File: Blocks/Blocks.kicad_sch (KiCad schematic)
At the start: 0 parts

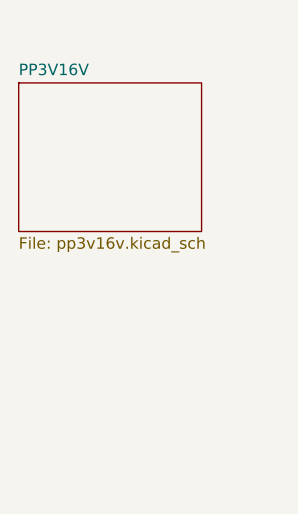
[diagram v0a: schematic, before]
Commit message: drop powermux
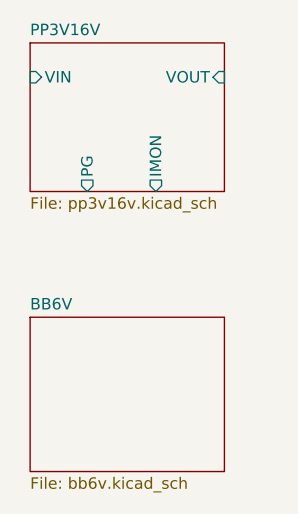
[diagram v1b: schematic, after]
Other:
- added sheet BB6V (bb6v.kicad_sch)
- sheet PP3V16V ports: added IMON, PG, VIN, VOUT; removed none
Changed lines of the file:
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@@
 	(paper "A4")
 	(sheet
-		(at 19.05 23.495)
-		(size 20.32 16.51)
+		(at 20.32 49.53)
+		(size 21.59 17.145)
+		(fields_autoplaced yes)
+		(stroke
+			(width 0.1524)
+			(type solid)
+		)
+		(fill
+			(color 0 0 0 0.0000)
+		)
+		(property "Sheetname" "BB6V"
+			(at 20.32 48.8184 0)
+			(effects
+				(font
+					(size 1.27 1.27)
+				)
+				(justify left bottom)
+			)
+		)
+		(property "Sheetfile" "bb6v.kicad_sch"
+			(at 20.32 67.2596 0)
+			(effects
+				(font
+					(size 1.27 1.27)
+				)
+				(justify left top)
+			)
+		)
+		(instances
+			(project "Blocks"
+				(path "/48ddfdd8-68fa-4e63-aa18-bc113cdf8cfa"
+					(page "3")
+				)
+			)
+		)
+	)
+	(sheet
+		(at 20.32 19.05)
+		(size 21.59 16.51)
 		(fields_autoplaced yes)
 		(stroke
@@
 		)
 		(property "Sheetname" "PP3V16V"
-			(at 19.05 22.7834 0)
+			(at 20.32 18.3384 0)
 			(effects
 				(font
@@
 		)
 		(property "Sheetfile" "pp3v16v.kicad_sch"
-			(at 19.05 40.5896 0)
+			(at 20.32 36.1446 0)
 			(effects
 				(font
@@
 			)
 		)
+		(pin "VIN" input
+			(at 20.32 22.86 180)
+			(effects
+				(font
+					(size 1.27 1.27)
+				)
+				(justify left)
+			)
+		)
+		(pin "PG" output
+			(at 26.67 35.56 270)
+			(effects
+				(font
+					(size 1.27 1.27)
+				)
+				(justify left)
+			)
+		)
+		(pin "VOUT" input
+			(at 41.91 22.86 0)
+			(effects
+				(font
+					(size 1.27 1.27)
+				)
+				(justify right)
+			)
+		)
+		(pin "IMON" output
+			(at 34.29 35.56 270)
+			(effects
+				(font
+					(size 1.27 1.27)
+				)
+				(justify left)
+			)
+		)

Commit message: BuckBoostTest v0.1
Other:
- sheet BB6V ports: added PG, VIN, VLogic, VOUT; removed none
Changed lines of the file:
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@@
+			)
+		)
+		(pin "VIN" input
+			(at 20.32 54.61 180)
+			(effects
+				(font
+					(size 1.27 1.27)
+				)
+				(justify left)
+			)
+		)
+		(pin "VOUT" input
+			(at 41.91 54.61 0)
+			(effects
+				(font
+					(size 1.27 1.27)
+				)
+				(justify right)
+			)
+		)
+		(pin "VLogic" input
+			(at 27.94 66.675 270)
+			(effects
+				(font
+					(size 1.27 1.27)
+				)
+				(justify left)
+			)
+		)
+		(pin "PG" output
+			(at 33.02 66.675 270)
+			(effects
+				(font
+					(size 1.27 1.27)
+				)
+				(justify left)
 			)
 		)

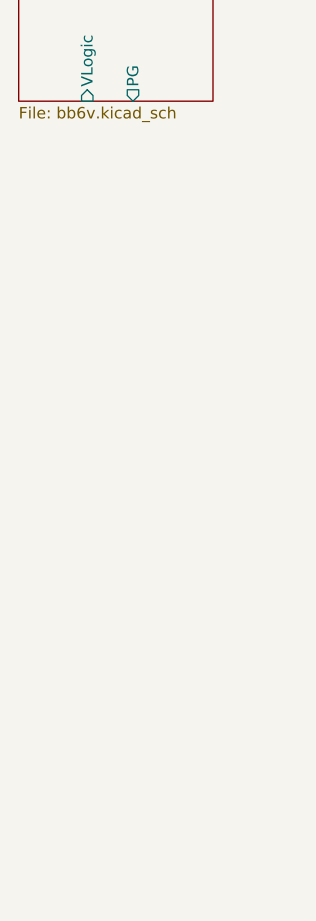
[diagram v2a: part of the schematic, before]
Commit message: add usb serial and start on ESP12
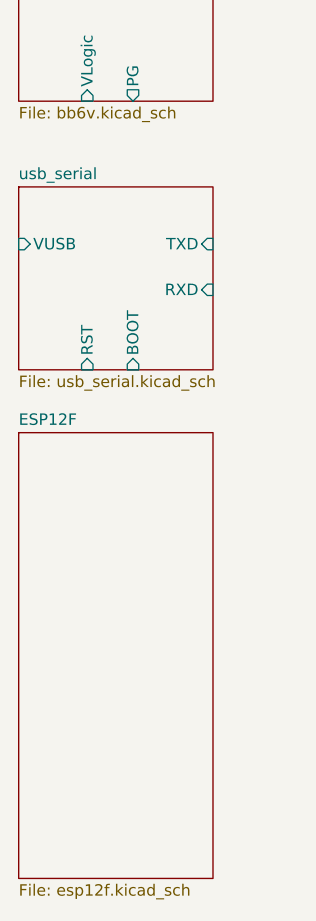
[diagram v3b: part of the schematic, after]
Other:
- added sheet ESP12F (esp12f.kicad_sch)
- added sheet usb_serial (usb_serial.kicad_sch)
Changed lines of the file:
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@@
+	)
+	(sheet
+		(at 20.32 76.2)
+		(size 21.59 20.32)
+		(fields_autoplaced yes)
+		(stroke
+			(width 0.1524)
+			(type solid)
+		)
+		(fill
+			(color 0 0 0 0.0000)
+		)
+		(property "Sheetname" "usb_serial"
+			(at 20.32 75.4884 0)
+			(effects
+				(font
+					(size 1.27 1.27)
+				)
+				(justify left bottom)
+			)
+		)
+		(property "Sheetfile" "usb_serial.kicad_sch"
+			(at 20.32 97.1046 0)
+			(effects
+				(font
+					(size 1.27 1.27)
+				)
+				(justify left top)
+			)
+		)
+		(pin "VUSB" input
+			(at 20.32 82.55 180)
+			(effects
+				(font
+					(size 1.27 1.27)
+				)
+				(justify left)
+			)
+		)
+		(pin "TXD" input
+			(at 41.91 82.55 0)
+			(effects
+				(font
+					(size 1.27 1.27)
+				)
+				(justify right)
+			)
+		)
+		(pin "RST" input
+			(at 27.94 96.52 270)
+			(effects
+				(font
+					(size 1.27 1.27)
+				)
+				(justify left)
+			)
+		)
+		(pin "BOOT" input
+			(at 33.02 96.52 270)
+			(effects
+				(font
+					(size 1.27 1.27)
+				)
+				(justify left)
+			)
+		)
+		(pin "RXD" input
+			(at 41.91 87.63 0)
+			(effects
+				(font
+					(size 1.27 1.27)
+				)
+				(justify right)
+			)
+		)
+		(instances
+			(project "Blocks"
+				(path "/48ddfdd8-68fa-4e63-aa18-bc113cdf8cfa"
+					(page "4")
+				)
+			)
+		)
 	)
 	(sheet
@@
 				)
 			)
+		)
+	)
+	(sheet
+		(at 20.32 103.505)
+		(size 21.59 49.53)
+		(fields_autoplaced yes)
+		(stroke
+			(width 0.1524)
+			(type solid)
+		)
+		(fill
+			(color 0 0 0 0.0000)
+		)
+		(property "Sheetname" "ESP12F"
+			(at 20.32 102.7934 0)
+			(effects
+				(font
+					(size 1.27 1.27)
+				)
+				(justify left bottom)
+			)
+		)
+		(property "Sheetfile" "esp12f.kicad_sch"
+			(at 20.32 153.6196 0)
+			(effects
+				(font
+					(size 1.27 1.27)
+				)
+				(justify left top)
+			)
+		)
+		(instances
+			(project "Blocks"
+				(path "/48ddfdd8-68fa-4e63-aa18-bc113cdf8cfa"
+					(page "5")
+				)
+			)

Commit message: add pins
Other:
- sheet ESP12F ports: added 3V3, BOOT, ONEW, RST, RXD, SCL, SDA, TXD; removed none
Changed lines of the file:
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@@
+			)
+		)
+		(pin "RXD" input
+			(at 20.32 118.11 180)
+			(effects
+				(font
+					(size 1.27 1.27)
+				)
+				(justify left)
+			)
+		)
+		(pin "TXD" input
+			(at 20.32 121.92 180)
+			(effects
+				(font
+					(size 1.27 1.27)
+				)
+				(justify left)
+			)
+		)
+		(pin "SDA" input
+			(at 41.91 118.11 0)
+			(effects
+				(font
+					(size 1.27 1.27)
+				)
+				(justify right)
+			)
+		)
+		(pin "BOOT" input
+			(at 20.32 125.73 180)
+			(effects
+				(font
+					(size 1.27 1.27)
+				)
+				(justify left)
+			)
+		)
+		(pin "SCL" input
+			(at 41.91 121.92 0)
+			(effects
+				(font
+					(size 1.27 1.27)
+				)
+				(justify right)
+			)
+		)
+		(pin "ONEW" input
+			(at 41.91 125.73 0)
+			(effects
+				(font
+					(size 1.27 1.27)
+				)
+				(justify right)
+			)
+		)
+		(pin "RST" input
+			(at 20.32 129.54 180)
+			(effects
+				(font
+					(size 1.27 1.27)
+				)
+				(justify left)
+			)
+		)
+		(pin "3V3" input
+			(at 20.32 107.95 180)
+			(effects
+				(font
+					(size 1.27 1.27)
+				)
+				(justify left)
 			)
 		)

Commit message: clean up
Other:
- added sheet LEDComparator (LED_comparator.kicad_sch)
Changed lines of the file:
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@@
 	(paper "A4")
+	(sheet
+		(at 55.88 17.78)
+		(size 19.05 17.78)
+		(fields_autoplaced yes)
+		(stroke
+			(width 0.1524)
+			(type solid)
+		)
+		(fill
+			(color 0 0 0 0.0000)
+		)
+		(property "Sheetname" "LEDComparator"
+			(at 55.88 17.0684 0)
+			(effects
+				(font
+					(size 1.27 1.27)
+				)
+				(justify left bottom)
+			)
+		)
+		(property "Sheetfile" "LED_comparator.kicad_sch"
+			(at 55.88 36.1446 0)
+			(effects
+				(font
+					(size 1.27 1.27)
+				)
+				(justify left top)
+			)
+		)
+		(instances
+			(project "Blocks"
+				(path "/48ddfdd8-68fa-4e63-aa18-bc113cdf8cfa"
+					(page "6")
+				)
+			)
+		)
+	)
 	(sheet
 		(at 20.32 49.53)
